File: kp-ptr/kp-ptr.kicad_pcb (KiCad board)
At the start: 4 copper layers, 31 x 100 mm, 173 parts, among them IC1 E22-900M22S, J1 ESP32_PROG_CON, J10 Conn_01x02, J11 Conn_01x02, J12 Conn_01x02, J13 Conn_01x02, J2 Conn_01x02, J3 Conn_01x02, J4 USB_C_Receptacle_USB2.0, J5 u.fl, J6 Conn_01x06_Male, J7 Conn_01x10_Male, J8 Conn_01x06_Male, J9 Conn_01x02_Male, Q1 NMOS_SOT23, Q2 DMC2025UFDB_v2, Q3 DMC2025UFDB_v2, Q4 DMC2025UFDB_v2, Q5 DMC2025UFDB_v2, U1 ESP32-S3FN8, U10 USBLC6-2SC6, U11 W25Q128JVS, U12 NL27WZU04DBVT1G, U2 MS560702BA03-50, U3 MMC5983MA, U4 H3LIS331, U5 L76-L, U6 NJG1156PCD, U7 LSM6DSO32, U8 AZ1117CH-5.0TRG1, U9 LDFM33PVR, Y1 7M40000005-40MHz

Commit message: PCB update to v1.0
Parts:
- R14: moved to F.Cu
- moved R14 6.51 mm to (148.3, 73.3)
- moved R59 3.25 mm to (151.9, 97.9), turned to 180 degrees
- moved R54 3.12 mm to (154.8, 112.7), turned to -90 degrees
- moved R44 2.80 mm to (154.8, 106.4), turned to -90 degrees
- moved R45 2.76 mm to (155.0, 118.6), turned to -90 degrees
- moved R13 1.33 mm to (151.7, 72.5)
- moved R48 1.27 mm to (154.8, 104.4), turned to 90 degrees
- moved R49 1.26 mm to (155.0, 116.7), turned to 90 degrees
- moved R12 1.15 mm to (150.4, 72.5)
- moved R11 1.07 mm to (149.3, 71.5)
- moved R58 0.92 mm to (154.8, 110.7), turned to 90 degrees
- moved R51 0.47 mm to (145.6, 114.9)
- moved C48 0.45 mm to (145.6, 115.9)
- moved R47 0.45 mm to (144.6, 120.0)
- moved R60 0.45 mm to (145.4, 108.8)
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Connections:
- U11 pad 9: (no net) -> Earth
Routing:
- net Net-(Q3-Pad3): track 2.04 -> 11.0 mm
- net Net-(Q2-Pad3): track 2.00 -> 10.8 mm
- net Net-(Q4-Pad3): track 2.00 -> 10.6 mm
- net Net-(D1-Pad2): track 1.37 -> 7.32 mm, vias 0 -> 1
- net Net-(Q5-Pad3): track 2.12 -> 7.48 mm
- net Net-(R14-Pad2): track 7.14 -> 2.06 mm, vias 1 -> 0
- net IGN2_EN: track 55.1 -> 59.4 mm
- net IGN1_EN: track 51.3 -> 55.1 mm
- net Net-(F5-Pad2): track 0.00 -> 3.77 mm
- net Net-(J12-Pad2): track 0.00 -> 3.76 mm
- net Net-(J11-Pad2): track 0.00 -> 3.75 mm
- net Net-(J10-Pad2): track 0.00 -> 3.62 mm
- net IGN4_EN: track 44.0 -> 47.5 mm
- net +3.3VADC: track 11.4 -> 9.02 mm, vias 4 -> 3
- net +3V3: track 63.3 -> 65.1 mm
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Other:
- board text added: "2022-08-10 v1.0"
- board text added: "KP-PTR v1.0"
- board text removed: "2022-06-26 rev 0"
- board text removed: "KP-PTR v0"

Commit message: Work in progress
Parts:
- C23, C24: value 4.7uF -> 10uF
- C25: value 56pF -> DNP
- C30: value DNP -> 56pF
- C35, C36: value 10u -> 10uF 6V3
- C37: value 1uF -> 100n
- C38: value 1uF -> 100n 50V
- C43: value 4u7 -> 10uF
- F1, F2, F3, F4, F5: footprint Fuse:Fuse_1210_3225Metric -> Fuse:Fuse_1206_3216Metric
- R19: value 100k -> 100k 1%
- R20: value 10k -> 10k 1%
- R23: value 20k -> 22k
- R26: value 100k -> 10k
- moved R30 1.07 mm to (145.8, 40.2), turned to -90 degrees
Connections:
- net IGN4_PWR renamed IGN1_PWR
- IC1 pad 13: unconnected-(IC1-Pad13) -> LED2
- J1 pad 2: Net-(J1-Pad2) -> U0RXD
- J1 pad 3: Net-(J1-Pad3) -> U0TXD
- J1 pad 4: Net-(J1-Pad4) -> BOOT_PIN
- R1 pad 1: BOOT_PIN -> IO0
- R1 pad 2: Net-(J1-Pad4) -> BOOT_PIN
- R3 pad 1: U0RXD -> IO44
- R3 pad 2: Net-(J1-Pad2) -> U0RXD
- R4 pad 1: U0TXD -> IO43
- R4 pad 2: Net-(J1-Pad3) -> U0TXD
- U1 pad 49: U0TXD -> IO43
- U1 pad 5: BOOT_PIN -> IO0
- U1 pad 50: U0RXD -> IO44
- U1 pad 52: LED2 -> IO46
- U11 pad 9: Earth -> (no net)
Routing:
- net IO0: track 0.00 -> 18.6 mm, vias 0 -> 2
- net IO43: track 0.00 -> 18.1 mm, vias 0 -> 2
- net BOOT_PIN: track 18.6 -> 0.89 mm, vias 2 -> 0
- net U0TXD: track 18.1 -> 0.89 mm, vias 2 -> 0
- net IO44: track 0.00 -> 16.9 mm, vias 0 -> 2
- net U0RXD: track 16.9 -> 0.89 mm, vias 2 -> 0
- net LED2: track 27.0 -> 16.7 mm, vias 0 -> 1
- net Net-(J1-Pad3): track 0.89 -> 0.00 mm
- net Net-(J1-Pad4): track 0.89 -> 0.00 mm
- net Net-(J1-Pad2): track 0.89 -> 0.00 mm

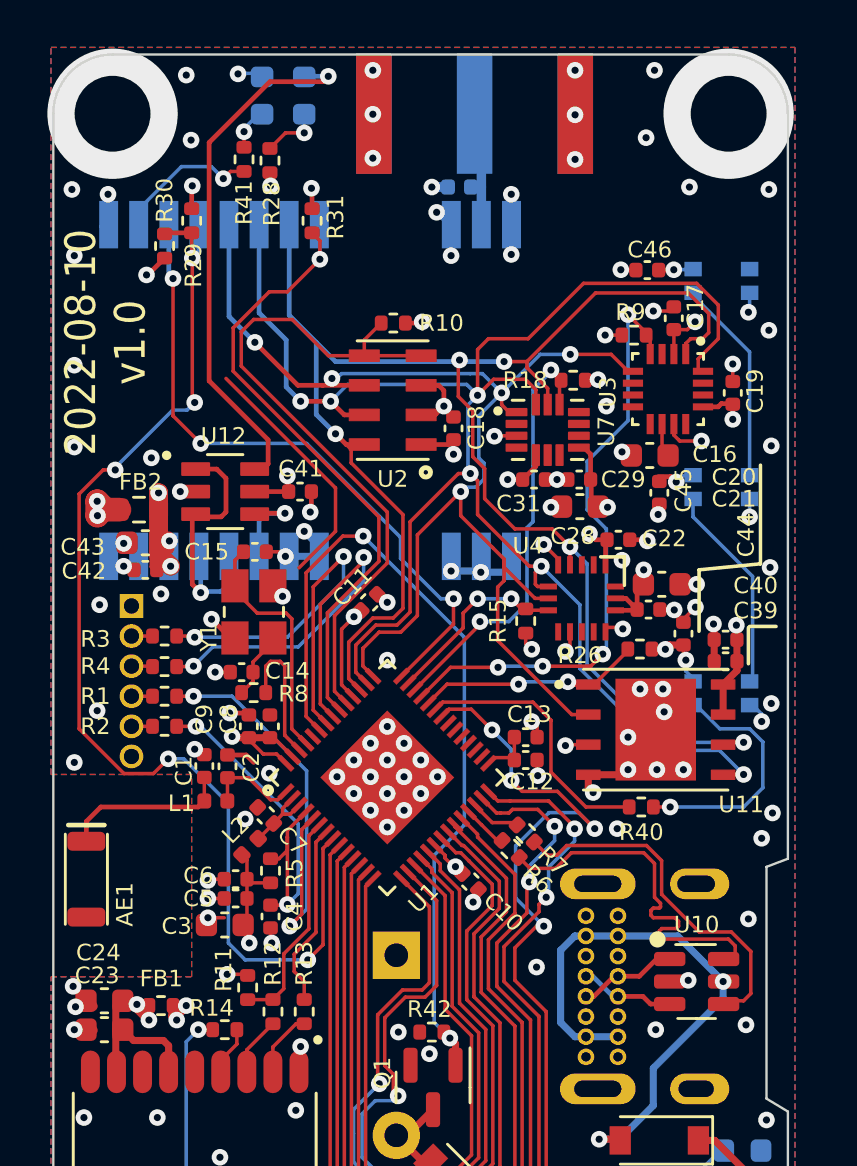
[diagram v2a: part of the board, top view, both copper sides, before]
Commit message: Second LSM added
Both LSM has INT connected
Small pins changes
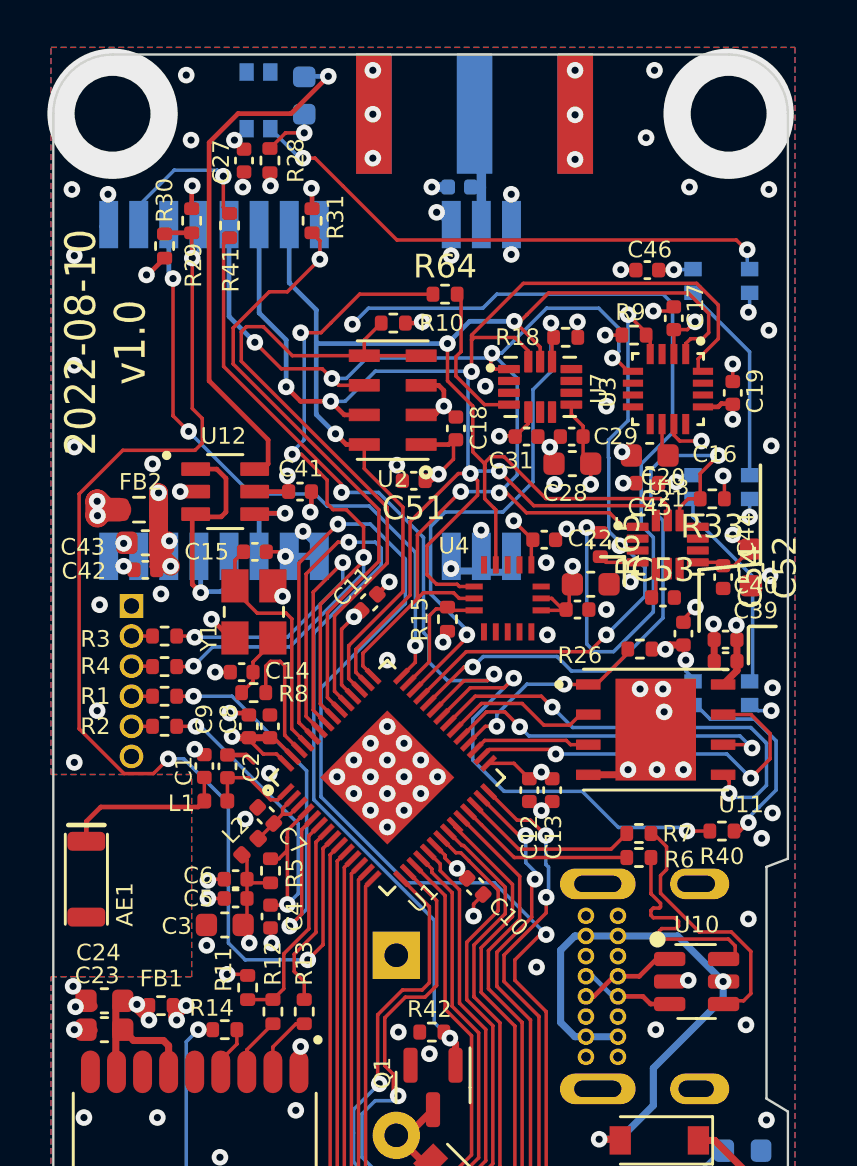
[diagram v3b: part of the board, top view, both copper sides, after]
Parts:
- added C27: 100nF, Capacitor_SMD:C_0402_1005Metric, F.Cu at (149.1, 36.6)
- added C51: 1uF, Capacitor_SMD:C_0402_1005Metric, F.Cu at (156.3, 50.1)
- added C52: 10uF, Capacitor_SMD:C_0603_1608Metric, F.Cu at (170.5, 53.7)
- added C53: 100nF, Capacitor_SMD:C_0402_1005Metric, F.Cu at (166.8, 55.0)
- added C54: 100nF, Capacitor_SMD:C_0402_1005Metric, F.Cu at (169.4, 54.2)
- added R33: 10k, Resistor_SMD:R_0402_1005Metric, F.Cu at (168.9, 50.9)
- added R64: 10k, Resistor_SMD:R_0402_1005Metric, F.Cu at (157.6, 42.2)
- added R65: 10k, Resistor_SMD:R_0402_1005Metric, F.Cu at (164.2, 52.8)
- added U13: LSM6DSO32, KP-PTR_lib:LSM6DSO32, F.Cu at (167.0, 52.8)
- D12: value LED -> WS2812B-2020; footprint LED_SMD:LED_0603_1608Metric -> KP-PTR_lib:WS2812B-2020
- R41: value 1k -> 10k
- U11: value W25Q128JVS -> W25Q256
- moved R6 5.42 mm to (165.8, 66.0), turned to 180 degrees
- moved R7 4.78 mm to (165.8, 65.0), turned to 180 degrees
- moved R40 3.55 mm to (169.3, 64.9)
- moved R15 3.30 mm to (157.7, 55.9)
- moved U4 3.13 mm to (160.3, 55.1)
- moved C22 3.13 mm to (161.8, 52.6)
- moved C20 3.00 mm to (163.8, 54.5)
- moved C21 3.00 mm to (163.2, 55.5)
- moved R41 2.86 mm to (148.5, 39.3)
- moved C13 2.50 mm to (162.2, 63.1), turned to -90 degrees
- moved C28 1.84 mm to (163.0, 49.4)
- moved C29 1.84 mm to (163.0, 48.2)
- moved C31 1.84 mm to (161.1, 48.2)
- moved R18 1.84 mm to (162.7, 44.0)
- moved U7 1.84 mm to (161.6, 46.1)
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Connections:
- D12 pad 1: Earth -> unconnected-(D12-Pad1)
- D12 pad 2: Net-(D12-Pad2) -> Earth
- D15 pad 1: unconnected-(D15-Pad1) -> Net-(D12-Pad3)
- IC1 pad 13: LED2 -> Net-(IC1-Pad13)
- R26 pad 2: SPI_CS_FLASH -> SPI0_CS
- R41 pad 1: Net-(D12-Pad2) -> Net-(IC1-Pad13)
- R41 pad 2: LED2 -> RF_DIO1
- U1 pad 30: unconnected-(U1-Pad30) -> SPI0_HOLD
- U1 pad 31: unconnected-(U1-Pad31) -> SPI0_WP
- U1 pad 32: unconnected-(U1-Pad32) -> SPI0_CS
- U1 pad 33: unconnected-(U1-Pad33) -> SPI0_CLK
- U1 pad 34: unconnected-(U1-Pad34) -> SPI0_DO
- U1 pad 35: unconnected-(U1-Pad35) -> SPI0_DI
- U1 pad 36: SERVO_EN -> LED1
- U1 pad 37: LED1 -> RF_DIO1
- U1 pad 38: SPI_CS_FLASH -> SPI_CS_LSM2
- U1 pad 52: IO46 -> SERVO_EN
- U11 pad 1: SPI_CS_FLASH -> SPI0_CS
- U11 pad 2: SPI_MISO -> SPI0_DO
- U11 pad 3: +3V3 -> SPI0_WP
- U11 pad 5: SPI_MOSI -> SPI0_DI
- U11 pad 6: SPI_CLK -> SPI0_CLK
- U11 pad 7: +3V3 -> SPI0_HOLD
- U7 pad 4: unconnected-(U7-Pad4) -> LSM_INT
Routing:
- net IO44: track 16.9 -> 64.1 mm, vias 2 -> 4
- net RF_DIO1: track 0.00 -> 28.9 mm, vias 0 -> 2
- net SPI_CS_LSM2: track 0.00 -> 25.1 mm, vias 0 -> 2
- net Net-(D12-Pad3): track 0.00 -> 23.1 mm, vias 0 -> 2
- net SPI0_DI: track 0.00 -> 19.3 mm, vias 0 -> 2
- net SERVO_EN: track 38.4 -> 57.3 mm, vias 4 -> 2
- net IO43: track 18.1 -> 35.7 mm, vias 2 -> 4
- net LED2: track 16.7 -> 0.00 mm, vias 1 -> 0
- net SPI0_HOLD: track 0.00 -> 16.5 mm, vias 0 -> 2
- net SPI0_CLK: track 0.00 -> 14.6 mm, vias 0 -> 2
- net Earth: track 77.0 -> 66.8 mm, vias 283 -> 278
- net SPI_CS_FLASH: track 9.50 -> 0.00 mm, vias 2 -> 0
- net SPI0_CS: track 0.00 -> 8.78 mm, vias 0 -> 2
- net SPI_CLK: track 73.1 -> 65.3 mm, vias 5 -> 3
- net LED1: track 11.4 -> 19.1 mm, vias 0 -> 2
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
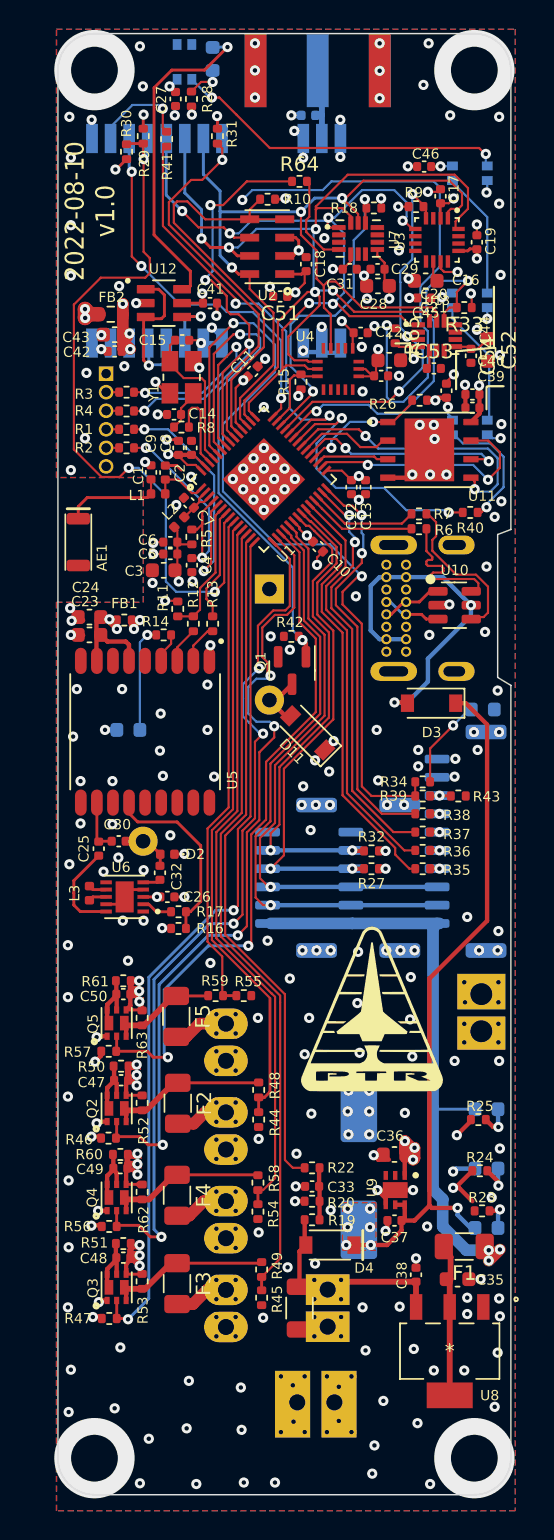
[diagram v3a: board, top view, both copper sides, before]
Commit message: IGN detector update
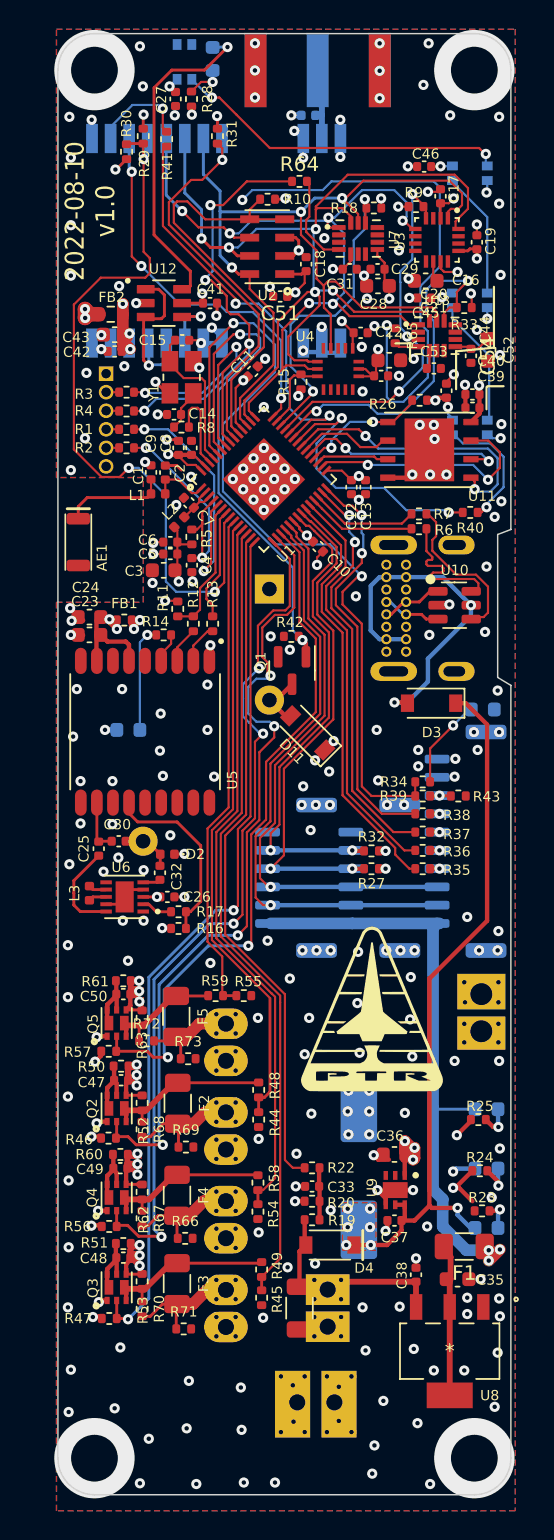
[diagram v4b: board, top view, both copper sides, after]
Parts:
- added R66: 2k5, Resistor_SMD:R_0402_1005Metric, F.Cu at (149.8, 114.6)
- added R67: 5k, Resistor_SMD:R_0402_1005Metric, F.Cu at (146.9, 113.2)
- added R68: 5k, Resistor_SMD:R_0402_1005Metric, F.Cu at (146.9, 107.1)
- added R69: 2k5, Resistor_SMD:R_0402_1005Metric, F.Cu at (149.9, 108.3)
- added R70: 5k, Resistor_SMD:R_0402_1005Metric, F.Cu at (146.9, 119.4)
- added R71: 2k5, Resistor_SMD:R_0402_1005Metric, F.Cu at (149.7, 120.8)
- added R72: 5k, Resistor_SMD:R_0402_1005Metric, F.Cu at (147.2, 101.0)
- added R73: 2k5, Resistor_SMD:R_0402_1005Metric, F.Cu at (150.0, 102.3)
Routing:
- net Net-(F3-Pad2): track 3.75 -> 8.21 mm
- net Net-(F2-Pad2): track 3.62 -> 8.04 mm
- net Net-(F4-Pad2): track 3.76 -> 8.00 mm
- net Net-(J13-Pad2): track 3.77 -> 7.03 mm
- net Net-(F5-Pad1): track 7.48 -> 8.63 mm
- net Net-(F3-Pad1): track 11.0 -> 11.8 mm
- net Net-(F4-Pad1): track 10.6 -> 11.4 mm
- net Net-(F2-Pad1): track 10.8 -> 11.6 mm

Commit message: JLC codes added
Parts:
- C12: value 0.1uF -> 100n
- U1: value ESP32-S3FN8 -> ESP32-S3
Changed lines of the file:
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@@
   (net 130 "Net-(D8-Pad1)")
   (net 131 "Net-(D9-Pad2)")
-  (net 132 "Net-(J13-Pad2)")
+  (net 132 "Net-(F5-Pad2)")
   (net 133 "Net-(F2-Pad1)")
   (net 134 "Net-(F2-Pad2)")
@@
       (effects (font (size 0.7 0.7) (thickness 0.15)))
     )
-    (fp_text value "0.1uF" (at 0 1.16 90) (layer "F.Fab")
+    (fp_text value "100n" (at 0 1.16 90) (layer "F.Fab")
       (effects (font (size 1 1) (thickness 0.15)))
     )
@@
       (effects (font (size 0.7 0.7) (thickness 0.15)))
     )
-    (fp_text value "ESP32-S3FN8" (at 8.6 5.635 45) (layer "F.Fab")
+    (fp_text value "ESP32-S3" (at 8.6 5.635 45) (layer "F.Fab")
       (effects (font (size 1 1) (thickness 0.15)))
     )
@@
       (net 139 "Net-(F5-Pad1)") (pintype "passive"))
     (pad "2" smd roundrect (at 1.4 0 270) (size 1.25 1.75) (layers "F.Cu" "F.Paste" "F.Mask") (roundrect_rratio 0.2)
-      (net 132 "Net-(J13-Pad2)") (pintype "passive"))
+      (net 132 "Net-(F5-Pad2)") (pintype "passive"))
     (model "${KICAD6_3DMODEL_DIR}/Fuse.3dshapes/Fuse_1206_3216Metric.wrl"
       (offset (xyz 0 0 0))
@@
       (net 139 "Net-(F5-Pad1)") (pintype "passive"))
     (pad "2" smd roundrect (at 0.51 0) (size 0.54 0.64) (layers "F.Cu" "F.Paste" "F.Mask") (roundrect_rratio 0.25)
-      (net 132 "Net-(J13-Pad2)") (pintype "passive"))
+      (net 132 "Net-(F5-Pad2)") (pintype "passive"))
     (model "${KICAD6_3DMODEL_DIR}/Resistor_SMD.3dshapes/R_0402_1005Metric.wrl"
       (offset (xyz 0 0 0))
@@
     (fp_line (start 0.525 -0.27) (end 0.525 0.27) (layer "F.Fab") (width 0.1))
     (pad "1" smd roundrect (at -0.51 0) (size 0.54 0.64) (layers "F.Cu" "F.Paste" "F.Mask") (roundrect_rratio 0.25)
-      (net 132 "Net-(J13-Pad2)") (pintype "passive"))
+      (net 132 "Net-(F5-Pad2)") (pintype "passive"))
     (pad "2" smd roundrect (at 0.51 0) (size 0.54 0.64) (layers "F.Cu" "F.Paste" "F.Mask") (roundrect_rratio 0.25)
       (net 1 "Earth") (pintype "passive"))
@@
       (net 1 "Earth") (pinfunction "Pin_1") (pintype "passive"))
     (pad "2" thru_hole roundrect (at 2.54 0 90) (size 2.1 3) (drill 1.1) (layers *.Cu *.Mask) (roundrect_rratio 0.5)
-      (net 132 "Net-(J13-Pad2)") (pinfunction "Pin_2") (pintype "passive"))
+      (net 132 "Net-(F5-Pad2)") (pinfunction "Pin_2") (pintype "passive"))
     (model "${KIPRJMOD}/3D models/282834-2--3DModel-STEP-1.STEP"
       (offset (xyz 1.25 -3.25 3))
